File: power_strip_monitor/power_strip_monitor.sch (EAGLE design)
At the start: 72 parts, among them U1 CS5467, U2 CS5467, U3 CS5467

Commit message: Finished schematic, starting component selection
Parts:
- added C28, C29, C30, C33, C34, C40, C41: .1u, SparkFun:CAP0603
- added C31, C32: 22p, SparkFun:CAP0603
- added C35: 2.2u, SparkFun:CAP0805
- added C36: 4700u, SparkFun:CAP_POLPTH2
- added C37: 1u, SparkFun:CAP0603
- added C38, C39: 10u, SparkFun:CAP0603
- added D1: (no value), diode:ZENER-DIODEZD-7.5
- added D2: BAS40, diode:BAS40
- added JP1: (no value), custom:FTDI_CABLESIP
- added JP2: AVR_SPI_PRG_6NS, SparkFun:AVR_SPI_PRG_6NS
- added Q1: 4.096MHz, SparkFun:CRYSTALSMD
- added R43, R47: 4.7k, SparkFun:RESISTOR0603
- added R44, R46, R48: 10k, SparkFun:RESISTOR0603
- added R45: 10, SparkFun:RESISTOR
- added TP1, TP10, TP11, TP12, TP13, TP14, TP15, TP16, TP17, TP18, TP19, TP2, TP20, TP3, TP4, TP5, TP6, TP7, TP8, TP9: TESTPOINTSMALLEST, WSNlib:TESTPOINTSMALLEST
- added TP21, TP22, TP23, TP24: TESTPOINT100MIL, WSNlib:TESTPOINT100MIL
- added U4: ATMEGA168, SparkFun:ATMEGA168
- added U6: XBEE-1B1, SparkFun:XBEE-1B1
- added U7, U8: V_REG_LDOSMD, SparkFun:V_REG_LDOSMD
- C1, C10, C11, C12, C13, C14, C15, C16, C17, C18, C19, C2, C20, C22, C23, C25, C26, C3, C4, C5, C6, C7, C8, C9: value (none) -> 10n; device SparkFun:CAP0805 -> SparkFun:CAP0603
- C21, C24, C27: device SparkFun:CAP0805 -> SparkFun:CAP0603
- R1, R10, R13, R16, R4, R7: value (none) -> 1m 1%
- R11, R12, R14, R15, R17, R18, R2, R3, R5, R6, R8, R9: value (none) -> 330 1%; device SparkFun:RESISTOR1206 -> SparkFun:RESISTOR0603
- R19, R20, R22, R23, R25, R26, R28, R29, R31, R32, R34, R35: value 330k -> 470k 320V
- R21, R24, R27, R30, R33, R36, R37, R38, R39, R40, R41, R42: value 1k -> 1k 1%; device SparkFun:RESISTOR1206 -> SparkFun:RESISTOR0603
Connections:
- removed net NEUTRAL: R1.1, R10.1, R12.2, R13.1, R15.2, R16.1, R18.2, R21.2, R3.2, R4.1, R6.2, R7.1, R9.2
- new net 3.3V: C38.2, C40.2, TP22.P$1, U6.VDD, U8.OUT
- new net ATMEGA_TO_XB: JP1.RXD, R43.2, R44.2, U6.DIN
- new net N$16: C31.1, Q1.2, U4.PB6(XTAL1/TOSC1)
- new net N$17: C32.1, Q1.1, U4.PB7(XTAL2/TOSC2)
- new net N$18: TP19.P$1, U4.ADC6
- new net N$19: TP20.P$1, U4.ADC7
- new net N$20: R43.1, U4.PD1(TXD)
- new net N$21: C36.+, C37.2, D2.C, TP23.P$1, U7.EN, U7.IN, U8.EN, U8.IN
- new net N$22: R47.1, U4.PD2(INT0)
- new net N$24: C35.2, D1.C, D2.A
- new net N$25: C35.1, R45.2
- new net RST: C41.1, JP2.5, R46.1, U4.PC6(/RESET)
- new net RTS#: C41.2, JP1.RTS
- new net XB_RESET: R47.2, R48.2, U6.RESET
- new net XB_TO_ATMEGA: JP1.TXD, U4.PD0(RXD), U6.DOUT
- net #CS1: now also U4.PC3(ADC3)
- net #CS2: now also U4.PC4(ADC4/SDA)
- net #CS3: now also U4.PC5(ADC5/SCL)
- net #INT1: now also U4.PC0(ADC0)
- net #INT2: now also U4.PC1(ADC1)
- net #INT3: now also U4.PC2(ADC2)
- net 5V: now also C33.2, C34.2, C39.2, JP1.VCC, JP2.2, R46.2, TP21.P$1, U4.AVCC, U4.VCC@1, U4.VCC@2, U7.OUT
- net GND: now also C28.1, C29.1, C30.1, C31.2, C32.2, C33.1, C34.1, C36.-, C37.1, C38.1, C39.1, C40.1, D1.A, JP1.CTS, JP1.GND, JP2.6, R1.1, R10.1, R12.2, R13.1, R15.2, R16.1, R18.2, R21.2, R3.2, R4.1, R44.1, R48.1, R6.2, R7.1, R9.2, TP24.P$1, U4.AGND, U4.GND@1, U4.GND@2, U6.GND, U6.RTS, U7.GND, U8.GND
- net HOT: now also R45.1
- net I1+: now also TP2.P$1
- net I1-: now also TP1.P$1
- net I2+: now also TP3.P$1
- net I2-: now also TP4.P$1
- net I3+: now also TP5.P$1
- net I3-: now also TP6.P$1
- net I4+: now also TP7.P$1
- net I4-: now also TP8.P$1
- net I5+: now also TP9.P$1
- net I5-: now also TP10.P$1
- net I6+: now also TP11.P$1
- net I6-: now also TP12.P$1
- net MISO: now also JP2.1, U4.PB4(MISO)
- net MOSI: now also JP2.4, U4.PB3(MOSI/OC2)
- net N$11: now also C29.2
- net N$14: now also C30.2
- net N$15: now also C28.2
- net SCLK: now also JP2.3, U4.PB5(SCK)
- net V1+: now also TP18.P$1
- net V2+: now also TP17.P$1
- net V3+: now also TP16.P$1
- net V4+: now also TP15.P$1
- net V5+: now also TP14.P$1
- net V6+: now also TP13.P$1
- net XIN: now also U4.PB0(ICP)
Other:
- note added: "Actual: 330.6mVpp (@220V)"
- note added: "Curr. Meas."
- note added: "Ideal: 1.76mOhm"
- note added: "NOTE: GND=NEUTRAL"
- note added: "Req: <500mVpp"
- note added: "Req: <50mVpp"
- note added: "Volt. Meas."
- note added: "Wattage: 400mW"

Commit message: Finding more parts
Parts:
- added R49: 4.7 200V, SparkFun:RESISTOR
- R19, R20, R22, R23, R25, R26, R28, R29, R31, R32, R34, R35: value 470k 320V -> 470k 200V
- R45: value 10 -> 4.7 200V
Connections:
- new net N$23: R45.2, R49.1
- net N$25: now also R49.2; no longer R45.2
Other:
- moved on the sheet: R45
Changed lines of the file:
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@@
 <part name="C12" library="SparkFun" deviceset="CAP" device="0603" value="10n"/>
 <part name="GND6" library="SparkFun" deviceset="GND" device=""/>
-<part name="R19" library="SparkFun" deviceset="RESISTOR" device="1206" value="470k 320V"/>
-<part name="R20" library="SparkFun" deviceset="RESISTOR" device="1206" value="470k 320V"/>
+<part name="R19" library="SparkFun" deviceset="RESISTOR" device="1206" value="470k 200V"/>
+<part name="R20" library="SparkFun" deviceset="RESISTOR" device="1206" value="470k 200V"/>
 <part name="R21" library="SparkFun" deviceset="RESISTOR" device="0603" value="1k 1%"/>
-<part name="R22" library="SparkFun" deviceset="RESISTOR" device="1206" value="470k 320V"/>
-<part name="R23" library="SparkFun" deviceset="RESISTOR" device="1206" value="470k 320V"/>
+<part name="R22" library="SparkFun" deviceset="RESISTOR" device="1206" value="470k 200V"/>
+<part name="R23" library="SparkFun" deviceset="RESISTOR" device="1206" value="470k 200V"/>
 <part name="R24" library="SparkFun" deviceset="RESISTOR" device="0603" value="1k 1%"/>
-<part name="R25" library="SparkFun" deviceset="RESISTOR" device="1206" value="470k 320V"/>
-<part name="R26" library="SparkFun" deviceset="RESISTOR" device="1206" value="470k 320V"/>
+<part name="R25" library="SparkFun" deviceset="RESISTOR" device="1206" value="470k 200V"/>
+<part name="R26" library="SparkFun" deviceset="RESISTOR" device="1206" value="470k 200V"/>
 <part name="R27" library="SparkFun" deviceset="RESISTOR" device="0603" value="1k 1%"/>
-<part name="R28" library="SparkFun" deviceset="RESISTOR" device="1206" value="470k 320V"/>
-<part name="R29" library="SparkFun" deviceset="RESISTOR" device="1206" value="470k 320V"/>
+<part name="R28" library="SparkFun" deviceset="RESISTOR" device="1206" value="470k 200V"/>
+<part name="R29" library="SparkFun" deviceset="RESISTOR" device="1206" value="470k 200V"/>
 <part name="R30" library="SparkFun" deviceset="RESISTOR" device="0603" value="1k 1%"/>
-<part name="R31" library="SparkFun" deviceset="RESISTOR" device="1206" value="470k 320V"/>
-<part name="R32" library="SparkFun" deviceset="RESISTOR" device="1206" value="470k 320V"/>
+<part name="R31" library="SparkFun" deviceset="RESISTOR" device="1206" value="470k 200V"/>
+<part name="R32" library="SparkFun" deviceset="RESISTOR" device="1206" value="470k 200V"/>
 <part name="R33" library="SparkFun" deviceset="RESISTOR" device="0603" value="1k 1%"/>
-<part name="R34" library="SparkFun" deviceset="RESISTOR" device="1206" value="470k 320V"/>
-<part name="R35" library="SparkFun" deviceset="RESISTOR" device="1206" value="470k 320V"/>
+<part name="R34" library="SparkFun" deviceset="RESISTOR" device="1206" value="470k 200V"/>
+<part name="R35" library="SparkFun" deviceset="RESISTOR" device="1206" value="470k 200V"/>
 <part name="R36" library="SparkFun" deviceset="RESISTOR" device="0603" value="1k 1%"/>
 <part name="GND7" library="SparkFun" deviceset="GND" device=""/>
@@
 <part name="R44" library="SparkFun" deviceset="RESISTOR" device="0603" value="10k"/>
 <part name="GND29" library="SparkFun" deviceset="GND" device=""/>
-<part name="R45" library="SparkFun" deviceset="RESISTOR" device="" value="10"/>
+<part name="R45" library="SparkFun" deviceset="RESISTOR" device="" value="4.7 200V"/>
 <part name="C35" library="SparkFun" deviceset="CAP" device="0805" value="2.2u"/>
 <part name="D1" library="diode" deviceset="ZENER-DIODE" device="ZD-7.5"/>
@@
 <part name="GND36" library="SparkFun" deviceset="GND" device=""/>
 <part name="GND37" library="SparkFun" deviceset="GND" device=""/>
+<part name="R49" library="SparkFun" deviceset="RESISTOR" device="" value="4.7 200V"/>
 </parts>
 <sheets>
@@
 <instance part="R44" gate="G$1" x="345.44" y="190.5" rot="R90"/>
 <instance part="GND29" gate="1" x="345.44" y="182.88"/>
-<instance part="R45" gate="G$1" x="81.28" y="307.34"/>
+<instance part="R45" gate="G$1" x="71.12" y="307.34"/>
 <instance part="C35" gate="G$1" x="96.52" y="307.34" rot="R90"/>
 <instance part="D1" gate="G$1" x="109.22" y="302.26" rot="R90"/>
@@
 <instance part="GND36" gate="1" x="370.84" y="180.34"/>
 <instance part="GND37" gate="1" x="327.66" y="101.6"/>
+<instance part="R49" gate="G$1" x="83.82" y="307.34"/>
 </instances>
 <busses>
@@
 <segment>
 <pinref part="R45" gate="G$1" pin="1"/>
-<wire x1="76.2" y1="307.34" x2="55.88" y2="307.34" width="0.1524" layer="91"/>
+<wire x1="66.04" y1="307.34" x2="55.88" y2="307.34" width="0.1524" layer="91"/>
 <label x="55.88" y="307.34" size="1.778" layer="95"/>
 </segment>
@@
 </segment>
 </net>
-<net name="N$25" class="0">
-<segment>
-<pinref part="C35" gate="G$1" pin="1"/>
-<pinref part="R45" gate="G$1" pin="2"/>
-<wire x1="91.44" y1="307.34" x2="86.36" y2="307.34" width="0.1524" layer="91"/>
-</segment>
-</net>
 <net name="RTS#" class="0">
 <segment>
@@
 </segment>
 </net>
+<net name="N$23" class="0">
+<segment>
+<pinref part="R45" gate="G$1" pin="2"/>
+<pinref part="R49" gate="G$1" pin="1"/>
+<wire x1="76.2" y1="307.34" x2="78.74" y2="307.34" width="0.1524" layer="91"/>
+</segment>
+</net>
+<net name="N$25" class="0">
+<segment>
+<pinref part="R49" gate="G$1" pin="2"/>
+<pinref part="C35" gate="G$1" pin="1"/>
+<wire x1="88.9" y1="307.34" x2="91.44" y2="307.34" width="0.1524" layer="91"/>
+</segment>
+</net>

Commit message: Saving power supply changes
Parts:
- C35: value 2.2u -> 1u
- C36: value 4700u -> 1m
- D1: value (none) -> 7.5V 200mW; device diode:ZENER-DIODEZD-7.5 -> Cool_Electricity:ZENER-DIODESOD-323
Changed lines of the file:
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@@
 <part name="GND29" library="SparkFun" deviceset="GND" device=""/>
 <part name="R45" library="SparkFun" deviceset="RESISTOR" device="" value="4.7 200V"/>
-<part name="C35" library="SparkFun" deviceset="CAP" device="0805" value="2.2u"/>
-<part name="D1" library="diode" deviceset="ZENER-DIODE" device="ZD-7.5"/>
+<part name="C35" library="SparkFun" deviceset="CAP" device="0805" value="1u"/>
+<part name="D1" library="Cool_Electricity" deviceset="ZENER-DIODE" device="SOD-323" value="7.5V 200mW"/>
 <part name="D2" library="diode" deviceset="BAS40" device=""/>
 <part name="GND30" library="SparkFun" deviceset="GND" device=""/>
-<part name="C36" library="SparkFun" deviceset="CAP_POL" device="PTH2" value="4700u"/>
+<part name="C36" library="SparkFun" deviceset="CAP_POL" device="PTH2" value="1m"/>
 <part name="C37" library="SparkFun" deviceset="CAP" device="0603" value="1u"/>
 <part name="C38" library="SparkFun" deviceset="CAP" device="0603" value="10u"/>

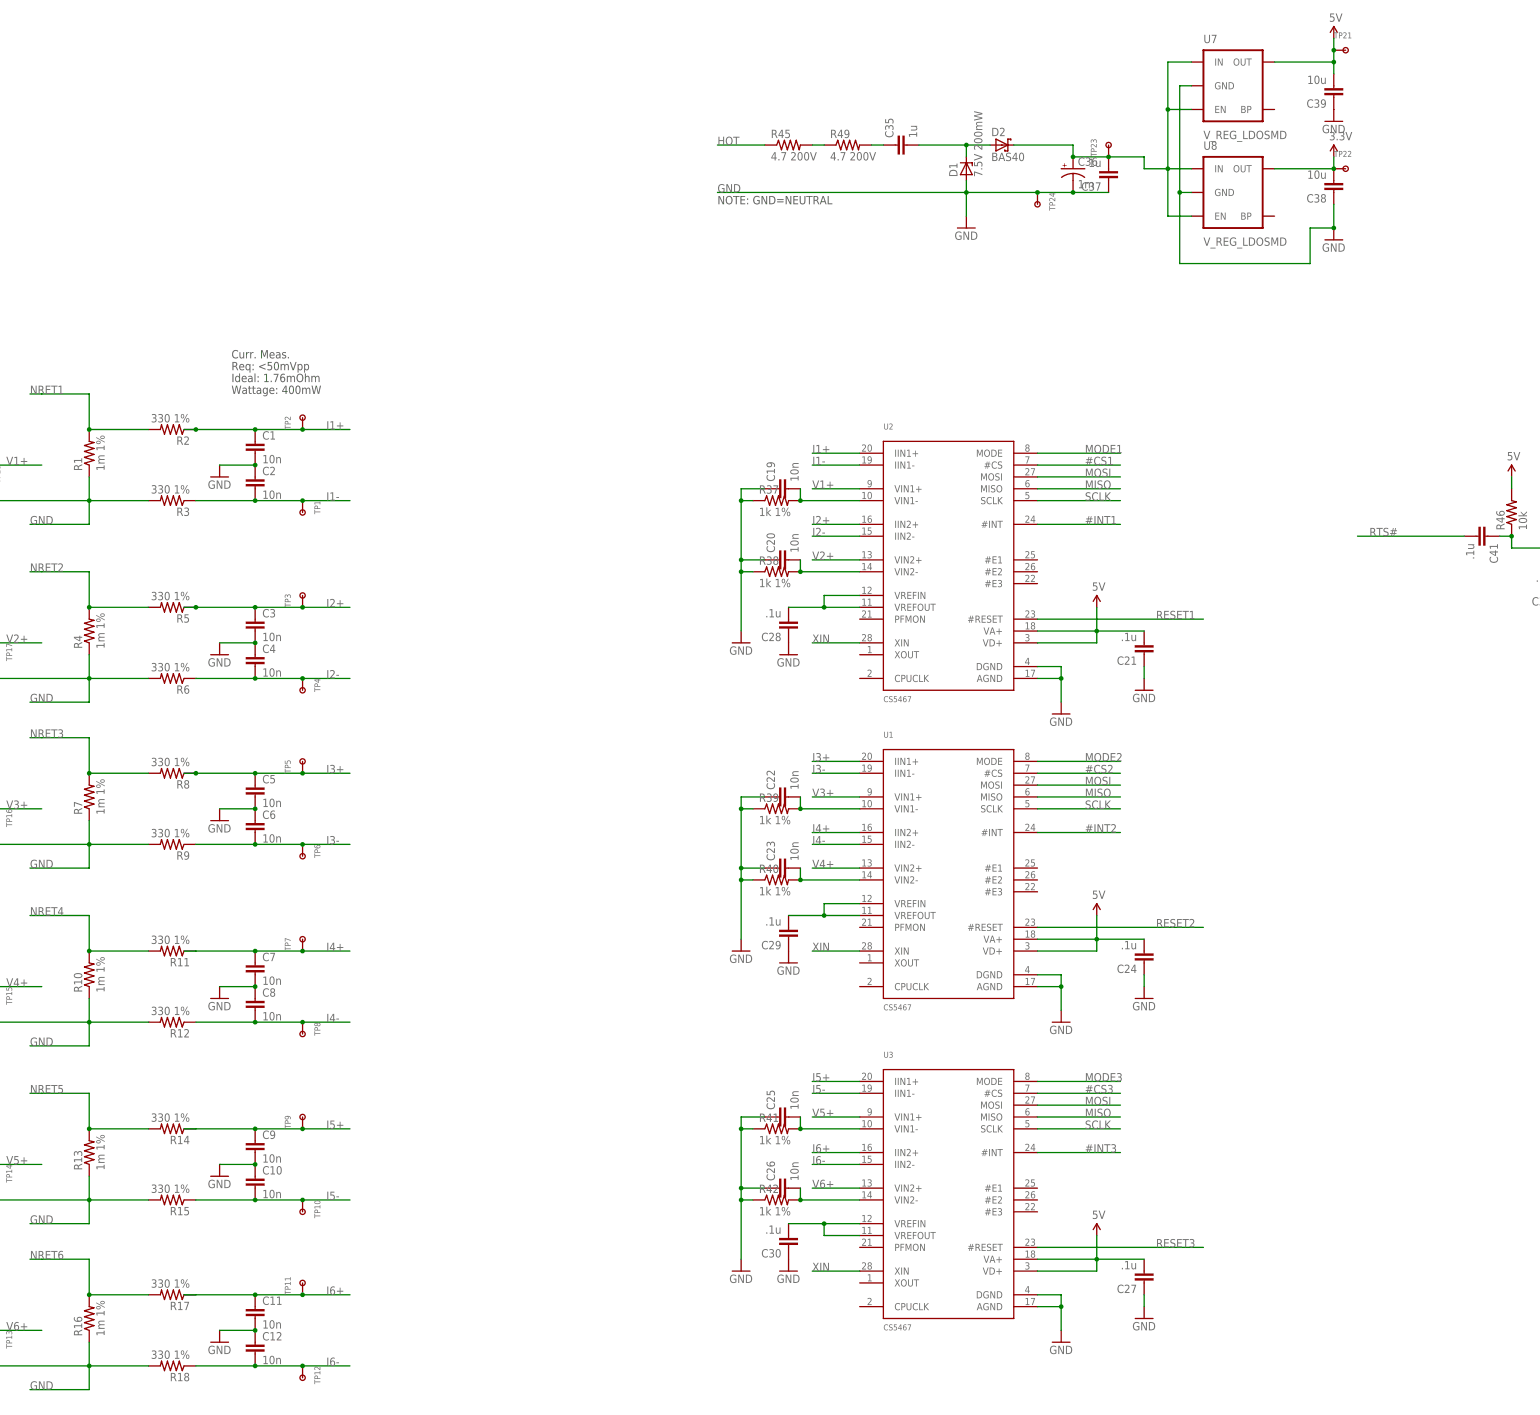
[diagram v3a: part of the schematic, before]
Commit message: Parts identified, new power supply
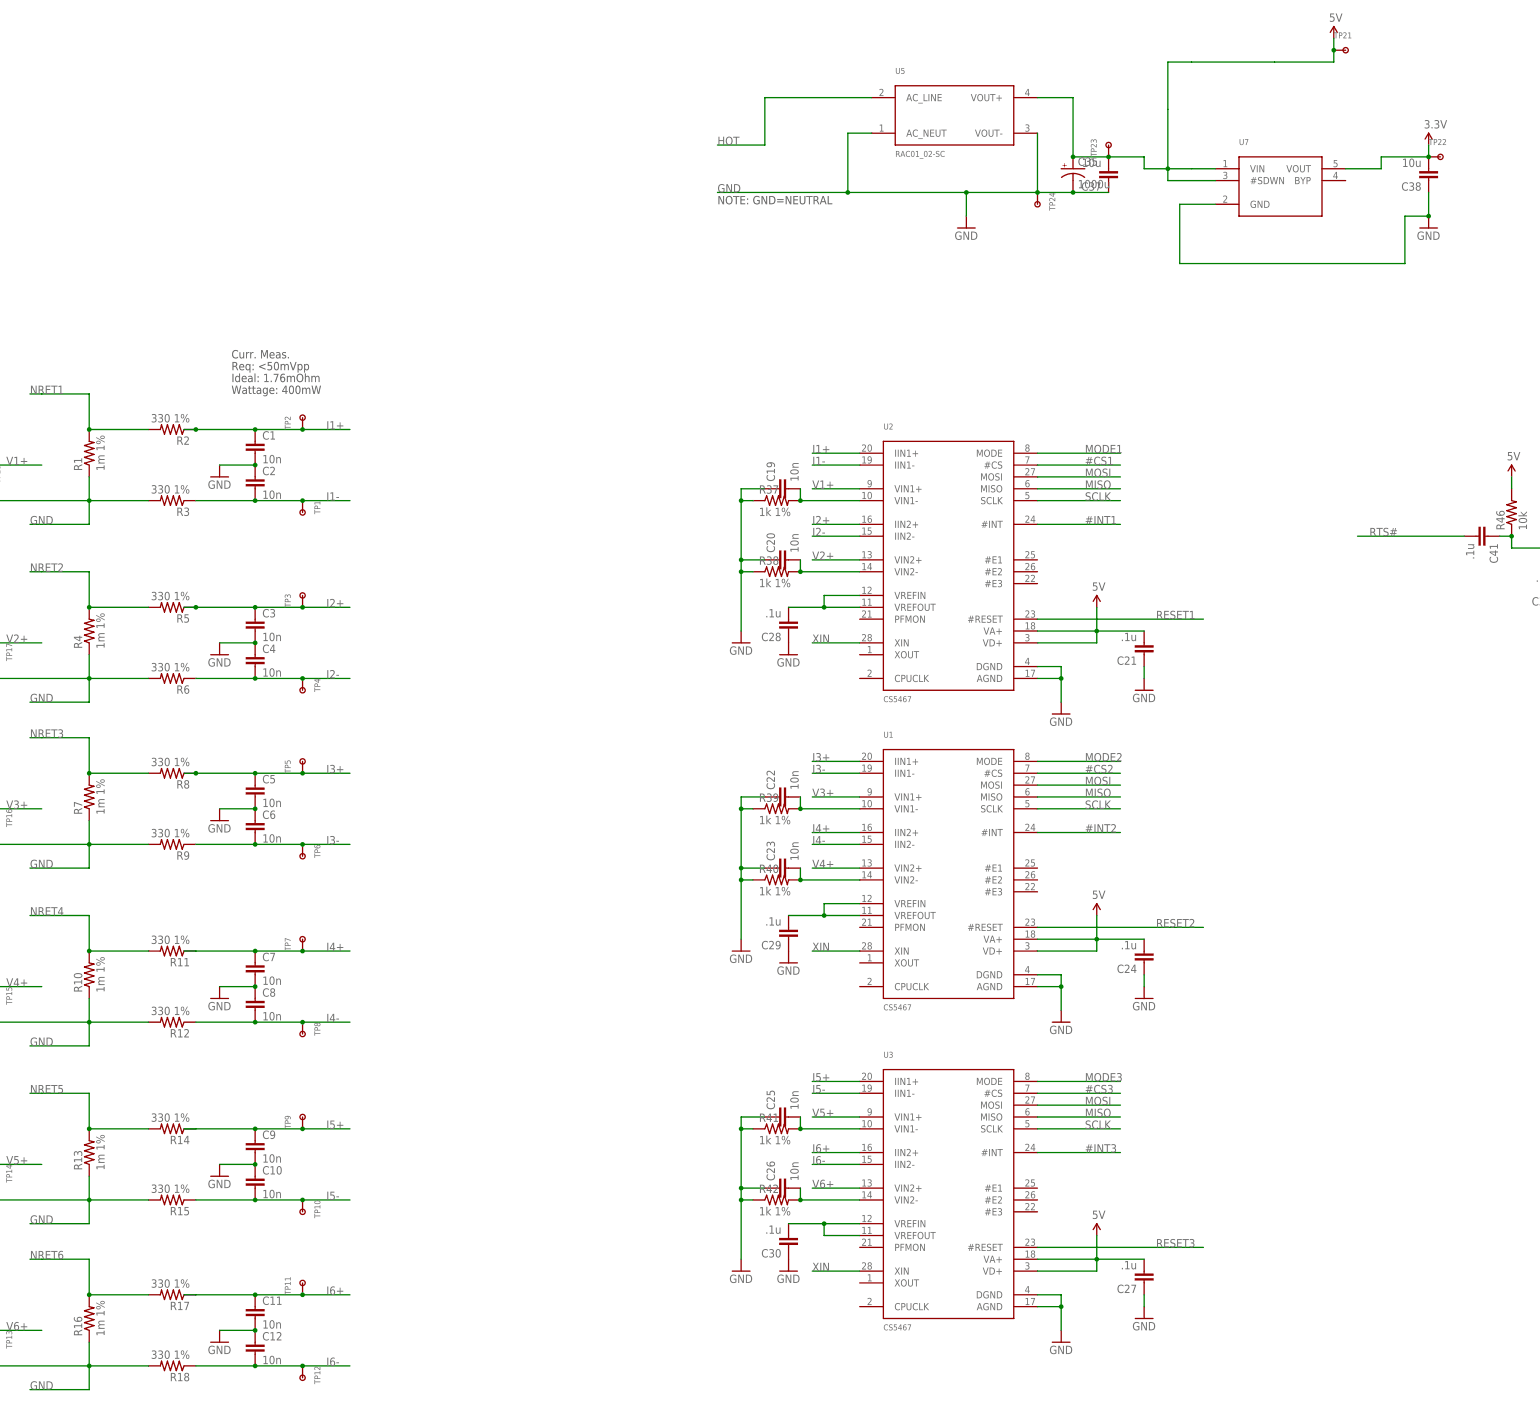
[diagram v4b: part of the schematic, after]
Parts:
- removed C36: 1m, SparkFun:CAP_POLPTH2
- removed C39: 10u, SparkFun:CAP0603
- removed D1: 7.5V 200mW, Cool_Electricity:ZENER-DIODESOD-323
- removed D2: BAS40, diode:BAS40
- removed R45, R49: 4.7 200V, SparkFun:RESISTOR
- removed U8: V_REG_LDOSMD, SparkFun:V_REG_LDOSMD
- added U5: RAC01_02-SC, Cool_Electricity:RAC01_02-SC
- C35: value 1u -> 1000u; device SparkFun:CAP0805 -> rcl_new:CPOL-USG
- C37: value 1u -> 10u
- R1, R10, R13, R16, R4, R7: device SparkFun:RESISTOR1206 -> rcl:R-US_R2512
- U7: value V_REG_LDOSMD -> (none); device SparkFun:V_REG_LDOSMD -> Cool_Electricity:LT1761-X
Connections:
- removed net N$21: C36.+, C37.2, D2.C, TP23.P$1, U7.EN, U7.IN, U8.EN, U8.IN
- removed net N$23: R45.2, R49.1
- removed net N$24: C35.2, D1.C, D2.A
- removed net N$25: C35.1, R49.2
- net 3.3V: now also U7.VOUT; no longer U8.OUT
- net 5V: now also C35.+, C37.2, TP23.P$1, U5.VOUT+, U7.#SDWN, U7.VIN; no longer C39.2, U7.OUT
- net GND: now also C35.-, U5.AC_NEUT, U5.VOUT-; no longer C36.-, C39.1, D1.A, U8.GND
- net HOT: now also U5.AC_LINE; no longer R45.1
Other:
- moved on the sheet: C38, TP22
